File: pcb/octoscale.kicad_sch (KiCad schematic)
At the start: 104 parts, among them J1 USB_C_Receptacle_USB2.0 TYPE-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, J2 Conn_01x04_Male, J3 Molex picoblade vertical C122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, J4 JST-SH, stemma, J5 JST-SH, J6 JST-SH, J7 Conn_01x04_Male, Q1 AO3415_C181094, Q2 MMBT44032T, Q3 S8050, SW1 SW_Push, SW2 SW_Push, SW3 SW_SPDT, U1 TP4065, U2 S-1172B33-E6T1U, U4 HX711, U5 ESP32-S3-WROOM-1

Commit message: basic schematic and pcb changes
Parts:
- removed JP2: SolderJumper_2_Bridged, Jumper:SolderJumper-2_P1.3mm_Bridged_RoundedPad1.0x1.5mm, symbol Jumper:SolderJumper_2_Bridged
- removed R15: 10K, Resistor_SMD:R_0805_2012Metric_Pad1.20x1.40mm_HandSolder, symbol Device:R_Small
- added D17: PMEG2010AEB, Diode_SMD:D_SOD-523, symbol easyeda2kicad:MSK4005
- R3: value 100k -> 1.5k
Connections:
- net +3V3: no longer C10.1, C12.1, C13.1, C14.1, C2.1, C28.2, C29.1, C8.1, C9.1, D14.2 (A), D15.1 (K), DS1.11 (BS1), DS1.13 (~{CS}), DS1.6 (VBAT), DS1.9 (VDD), J4.2 (Pin_2), J5.2 (Pin_2), J6.2 (Pin_2), LS1.1, Q2.2 (E), R10.1, R18.1, R19.1, TP12.1, U2.1 (VOUT), U4.1 (VSUP), U4.16 (DVDD), U5.2 (3V3)
- net +BATT: no longer C19.1, C20.1, C21.1, C22.1, C23.1, C24.1, C25.1, C26.1, C27.1, D1.2 (VDD), D10.2 (VDD), D11.2 (VDD), D12.2 (VDD), D3.2 (VDD), D6.2 (VDD), D7.2 (VDD), D8.2 (VDD), D9.2 (VDD)
- net LDO_EN: now also D17.1
- net VBUS: now also D17.2
- new net +3.3V: C10.1, C12.1, C13.1, C14.1, C19.1, C2.1, C20.1, C21.1, C22.1, C23.1, C24.1, C25.1, C26.1, C27.1, C28.2, C29.1, C8.1, C9.1, D1.2 (VDD), D10.2 (VDD), D11.2 (VDD), D12.2 (VDD), D14.2 (A), D15.1 (K), D3.2 (VDD), D6.2 (VDD), D7.2 (VDD), D8.2 (VDD), D9.2 (VDD), DS1.11 (BS1), DS1.13 (~{CS}), DS1.6 (VBAT), DS1.9 (VDD), J4.2 (Pin_2), J5.2 (Pin_2), J6.2 (Pin_2), LS1.1, Q2.2 (E), R10.1, R18.1, R19.1, TP12.1, U2.1 (VOUT), U4.1 (VSUP), U4.16 (DVDD), U5.2 (3V3)
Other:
- moved on the sheet: C12, C13, C14, D14, D16, D2, J4, R13, R18, R19, R21, SW3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

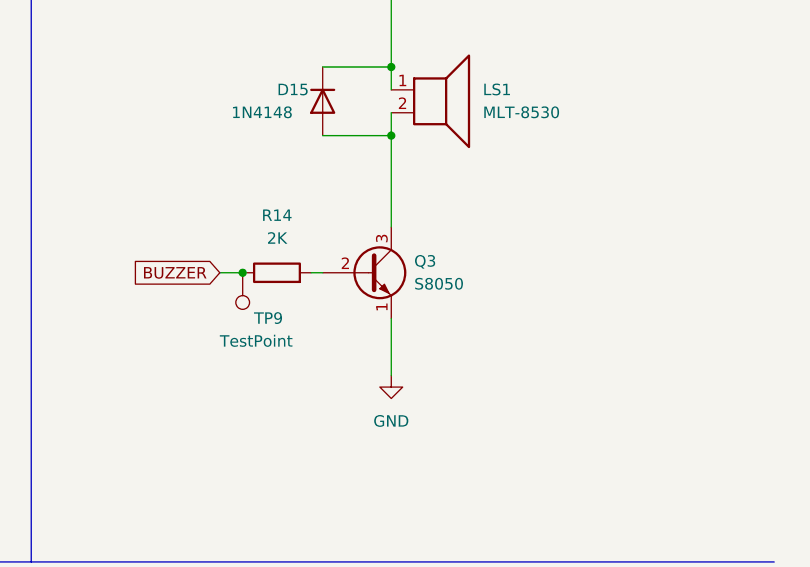
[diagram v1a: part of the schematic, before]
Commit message: fix speaker transistor
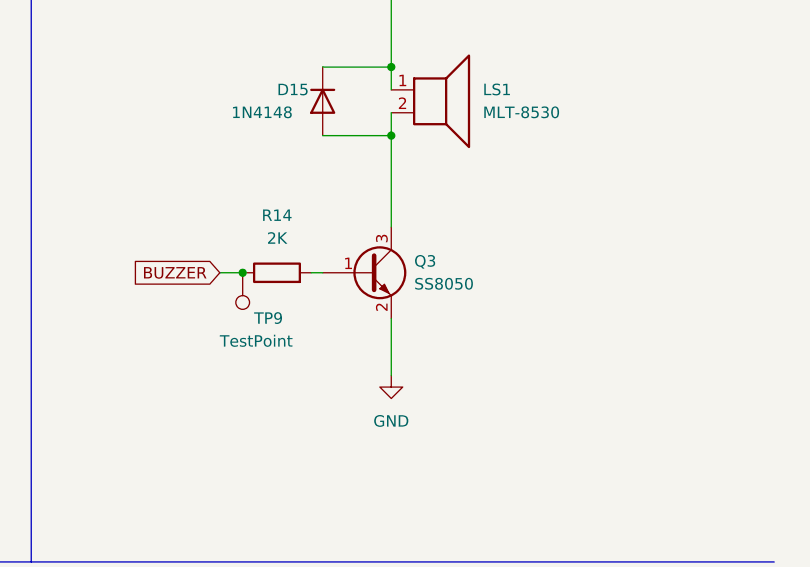
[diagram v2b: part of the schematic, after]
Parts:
- Q3: value S8050 -> SS8050; footprint Package_TO_SOT_SMD:TSOT-23 -> Package_TO_SOT_SMD:SOT-23; symbol Transistor_BJT:S8050 -> Transistor_BJT:MMBT5550L
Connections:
- net GND: now also Q3.2 (E); no longer Q3.1 (E)
- net at R14.2: now also Q3.1 (B); no longer Q3.2 (B)
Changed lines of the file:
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@@
     (pin "1")
   )
-  (symbol (lib_id "Transistor_BJT:S8050") (at 363.22 77.724 0) (unit 1)
+  (symbol (lib_id "Transistor_BJT:MMBT5550L") (at 363.22 77.724 0) (unit 1)
     (in_bom yes) (on_board yes) (fields_autoplaced)
     (property "Reference" "Q3" (id 0) (at 368.3 76.4539 0)
       (effects (font (size 1.27 1.27)) (justify left))
     )
-    (property "Value" "S8050" (id 1) (at 368.3 78.9939 0)
-      (effects (font (size 1.27 1.27)) (justify left))
-    )
-    (property "Footprint" "Package_TO_SOT_SMD:TSOT-23" (id 2) (at 368.3 79.629 0)
+    (property "Value" "SS8050" (id 1) (at 368.3 78.9939 0)
+      (effects (font (size 1.27 1.27)) (justify left))
+    )
+    (property "Footprint" "Package_TO_SOT_SMD:SOT-23" (id 2) (at 368.3 79.629 0)
       (effects (font (size 1.27 1.27) italic) (justify left) hide)
     )
-    (property "Datasheet" "http://www.unisonic.com.tw/datasheet/S8050.pdf" (id 3) (at 363.22 77.724 0)
+    (property "Datasheet" "www.onsemi.com/pub/Collateral/MMBT5550LT1-D.PDF" (id 3) (at 363.22 77.724 0)
       (effects (font (size 1.27 1.27)) (justify left) hide)
     )
@@
     )
     (path "/6361ce4c-5622-41ae-87b4-4eaace877734"
-      (reference "Q3") (unit 1) (value "S8050") (footprint "Package_TO_SOT_SMD:TSOT-23")
+      (reference "Q3") (unit 1) (value "SS8050") (footprint "Package_TO_SOT_SMD:SOT-23")
     )
     (path "/4d3b118c-bc8a-44bc-9f6f-cbadfe48ef2a"

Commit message: Fix buzzer footprint
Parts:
- LS1: footprint Buzzer_Beeper:Buzzer_CUI_CPT-9019S-SMT -> Buzzer_Beeper:MagneticBuzzer_Kobitone_254-EMB84Q-RO
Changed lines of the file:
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@@
       (effects (font (size 1.27 1.27)) (justify left))
     )
-    (property "Footprint" "Buzzer_Beeper:Buzzer_CUI_CPT-9019S-SMT" (id 2) (at 370.84 62.484 0)
+    (property "Footprint" "Buzzer_Beeper:MagneticBuzzer_Kobitone_254-EMB84Q-RO" (id 2) (at 370.84 62.484 0)
       (effects (font (size 1.27 1.27)) hide)
     )
@@
     )
     (path "/25a2f8bb-8f78-45c9-98fb-96b5fc7ff6f5"
-      (reference "LS1") (unit 1) (value "MLT-8530") (footprint "Buzzer_Beeper:Buzzer_CUI_CPT-9019S-SMT")
+      (reference "LS1") (unit 1) (value "MLT-8530") (footprint "Buzzer_Beeper:MagneticBuzzer_Kobitone_254-EMB84Q-RO")
     )
     (path "/c37e8969-7aa1-405c-ac57-11bcdd0d562b"

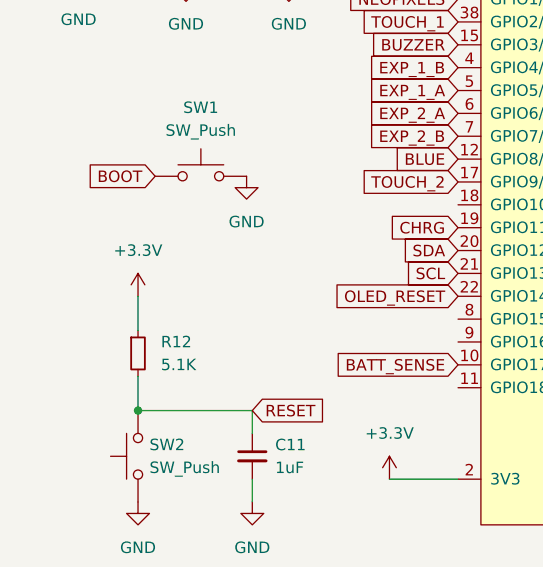
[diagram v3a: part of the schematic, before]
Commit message: Fix drc errors
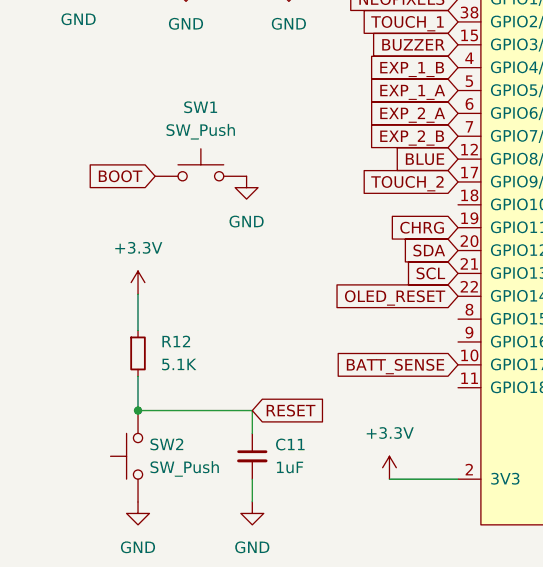
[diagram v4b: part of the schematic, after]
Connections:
- net +3V3 is gone; now on net +3.3V: R12.1
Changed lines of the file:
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@@
     (stroke (width 0) (type default) (color 0 0 0 0))
   )
-  (wire (pts (xy 24.13 198.12) (xy 24.13 201.93))
-    (stroke (width 0) (type default) (color 0 0 0 0))
-  )
   (wire (pts (xy 365.76 62.484) (xy 365.76 72.644))
     (stroke (width 0) (type default) (color 0 0 0 0))
@@
     (stroke (width 0) (type default) (color 0 0 0 0))
   )
+  (wire (pts (xy 24.13 197.866) (xy 24.13 201.93))
+    (stroke (width 0) (type default) (color 0 0 0 0))
+  )
   (wire (pts (xy 246.38 94.234) (xy 257.81 94.234))
     (stroke (width 0) (type default) (color 0 0 0 0))
@@
     (pin "2")
   )
-  (symbol (lib_id "power:+3.3V") (at 24.13 198.12 0) (unit 1)
-    (in_bom yes) (on_board yes) (fields_autoplaced)
-    (property "Reference" "#PWR027" (id 0) (at 24.13 201.93 0)
-      (effects (font (size 1.27 1.27)) hide)
-    )
-    (property "Value" "+3.3V" (id 1) (at 24.13 193.04 0))
-    (property "Footprint" "" (id 2) (at 24.13 198.12 0)
-      (effects (font (size 1.27 1.27)) hide)
-    )
-    (property "Datasheet" "" (id 3) (at 24.13 198.12 0)
-      (effects (font (size 1.27 1.27)) hide)
-    )
-    (pin "1")
-  )
   (symbol (lib_id "power:GND") (at 282.575 261.62 0) (unit 1)
     (in_bom yes) (on_board yes) (fields_autoplaced)
@@
     (pin "2")
   )
+  (symbol (lib_id "power:+3.3V") (at 24.13 197.866 0) (unit 1)
+    (in_bom yes) (on_board yes) (fields_autoplaced)
+    (property "Reference" "#PWR0131" (id 0) (at 24.13 201.676 0)
+      (effects (font (size 1.27 1.27)) hide)
+    )
+    (property "Value" "+3.3V" (id 1) (at 24.13 192.786 0))
+    (property "Footprint" "" (id 2) (at 24.13 197.866 0)
+      (effects (font (size 1.27 1.27)) hide)
+    )
+    (property "Datasheet" "" (id 3) (at 24.13 197.866 0)
+      (effects (font (size 1.27 1.27)) hide)
+    )
+    (pin "1")
+  )
   (symbol (lib_id "Device:R_Small") (at 232.41 94.234 90) (unit 1)
     (in_bom yes) (on_board yes)
@@
       (reference "#PWR026") (unit 1) (value "GND") (footprint "")
     )
-    (path "/77bceeaa-c057-4e31-846f-ba1616edfe0a"
-      (reference "#PWR027") (unit 1) (value "+3.3V") (footprint "")
-    )
     (path "/48ef2d1a-e8cd-48b5-b4eb-d6dff812055e"
       (reference "#PWR028") (unit 1) (value "GND") (footprint "")
@@
       (reference "#PWR0130") (unit 1) (value "+3.3V") (footprint "")
     )
+    (path "/daf66544-7c63-49bf-b871-7628b6d6cc60"
+      (reference "#PWR0131") (unit 1) (value "+3.3V") (footprint "")
+    )
     (path "/649edeef-7814-4a0f-8b14-912915793428"
